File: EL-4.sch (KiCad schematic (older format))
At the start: 17 parts, among them J1 Conn_01x02, J2 Conn_01x03, Q1 BSS214NW, Q2 BSS214NW, U1 MIC4832

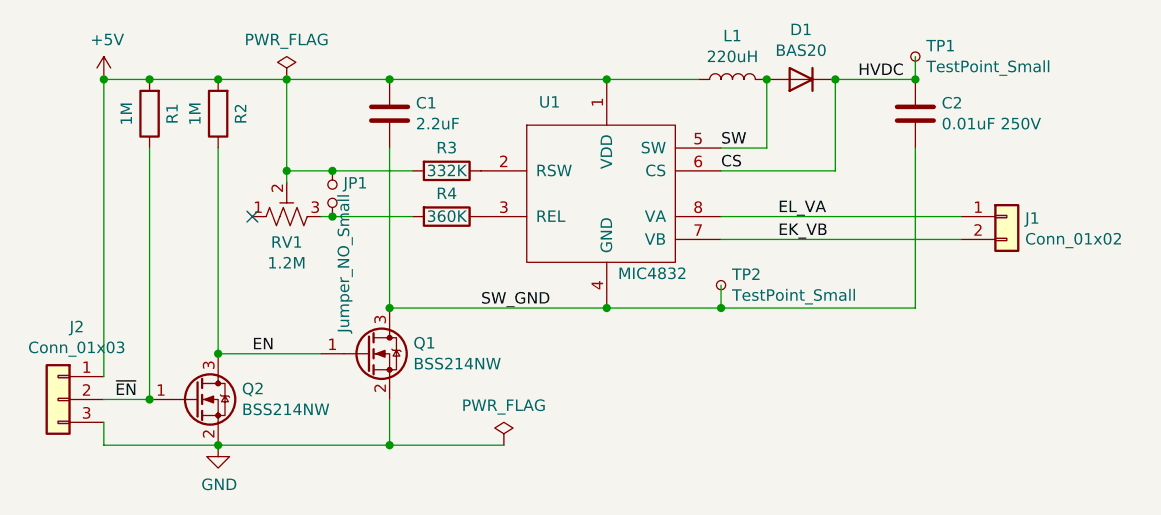
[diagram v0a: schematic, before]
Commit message: Version 1.0.
Changed enable method to pull RSW R3 to ground.
Changed R3, R4, R5 and C2 for 100Hz operation for 3 square inches.
Added input filter cap.

Also added BOM.

Signed-off-by: Aaron Williams <aaron.w2@gmail.com>
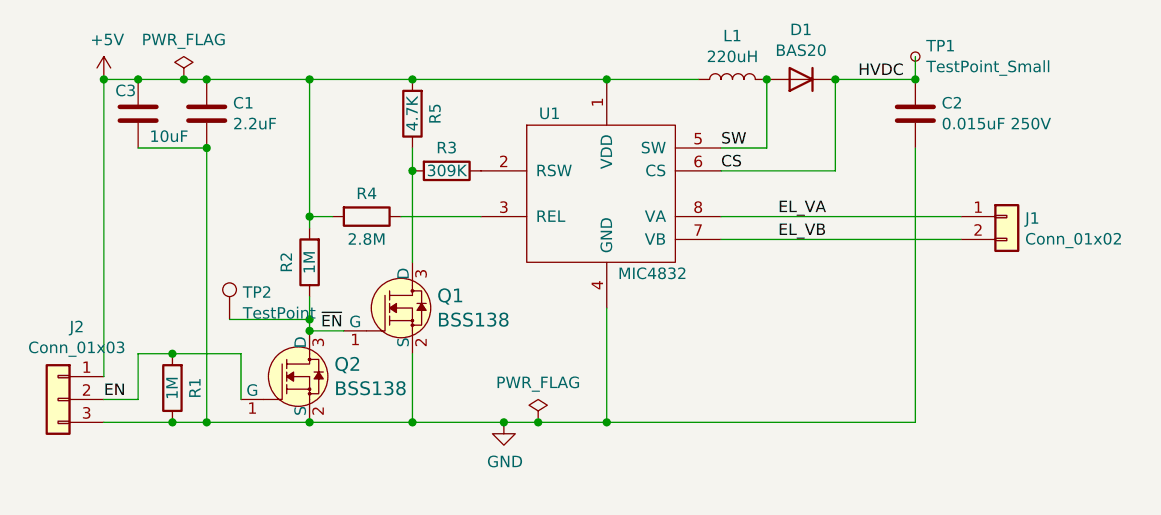
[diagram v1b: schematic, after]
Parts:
- removed JP1: Jumper_NO_Small, Jumper:SolderJumper-2_P1.3mm_Open_RoundedPad1.0x1.5mm, symbol Device:Jumper_NO_Small
- removed Q1, Q2: BSS214NW, Package_TO_SOT_SMD:SOT-323_SC-70, symbol Transistor_FET:BSS214NW
- removed RV1: 1.2M, Potentiometer_THT:Potentiometer_Bourns_3296W_Vertical, symbol Device:R_POT_TRIM_US
- removed TP2: TestPoint_Small, TestPoint:TestPoint_Pad_D1.0mm, symbol Connector:TestPoint_Small
- added C3: 10uF, Capacitor_SMD:C_0603_1608Metric, symbol Device:C
- added Q1, Q2: BSS138, Package_TO_SOT_SMD:SOT-23, symbol dk_Transistors-FETs-MOSFETs-Single:BSS138
- added R5: 4.7K, Resistor_SMD:R_0603_1608Metric, symbol Device:R
- added TP2: TestPoint, TestPoint:TestPoint_Pad_D1.0mm, symbol Connector:TestPoint
- C1: DESC (none) -> -; MFR (none) -> Yageo; MPN (none) -> CC0603MRY5V7BB225; SPN (none) -> 311-3415-1-ND; SPR (none) -> Digikey; SPURL (none) -> -
- C2: value 0.01uF 250V -> 0.015uF 250V; MPN C1206C103JAGACAUTO -> C1206C153KARECAUTO; SPN 80-C1206C103JAGAUTO -> 399-17899-1-ND; SPR Mouser -> Digikey; SPURL https://www.mouser.com/ProductDetail/KEMET/C1206C103JAGACAU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 -> https://www.digikey.com/en/products/detail/kemet/C1206C153K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
- D1: DESC (none) -> Diode Standard 200V 200mA Surface Mount SOT-23-3 (TO-236); MFR (none) -> ON Semiconductor; MPN (none) -> BAS20; SPN (none) -> BAS20FSCT-ND; SPR (none) -> Digikey; SPURL (none) -> https://www.digikey.com/en/products/detail/on-semiconductor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
- J1: DESC (none) -> Connector Header Through Hole 3 position 0.098; MFR (none) -> JST Sales America Inc.; MPN (none) -> B2B-XH-A-GU; SPN (none) -> 455-2946-ND; SPR (none) -> Digikey; SPURL (none) -> https://www.digikey.com/en/products/detail/jst-sales-americ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
- J2: DESC (none) -> Connector Header Through Hole 3 position 0.098; MFR (none) -> JST Sales America Inc.; MPN (none) -> B3B-XH-AM(LF)(SN); SPN (none) -> 455-2231-ND; SPR (none) -> Digikey; SPURL (none) -> https://www.digikey.com/en/products/detail/jst-sales-americ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
- L1: DESC (none) -> 220µH Semi-Shielded Wirewound Inductor 850mA 610mOhm Nonsta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; MFR (none) -> Bourns Inc.; MPN (none) -> SRN8040TA-221M; SPN (none) -> SRN8040TA-221MCT-ND; SPR (none) -> Digikey; SPURL (none) -> https://www.digikey.com/en/products/detail/bourns-inc/SRN80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
- R1, R2: DESC (none) -> 1 MOhms ±1% 0.1W, 1/10W Chip Resistor 0603 (1608 Metric) Au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; MFR (none) -> Stackpole Electronics Inc; MPN (none) -> RMCF0603FT1M00; SPN (none) -> RMCF0603FT1M00CT-ND; SPR (none) -> Digikey; SPURL (none) -> https://www.digikey.com/en/products/detail/stackpole-electr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
- R3: value 332K -> 309K; DESC (none) -> RES SMD 309K OHM 1% 1/10W 0603; MFR (none) -> Panasonic Electronic Components; MPN (none) -> ERJ-3EKF3093V; SPN (none) -> P309KHCT-ND; SPR (none) -> Digikey; SPURL (none) -> https://www.digikey.com/en/products/detail/panasonic-electr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
- R4: value 360K -> 2.8M; DESC (none) -> 2.8 MOhms ±1% 0.1W, 1/10W Chip Resistor 0603 (1608 Metric) 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; MFR Yageo -> Vishay Dale; MPN RC0603FR-07360KL -> CRCW06032M80FKEA; SPN (none) -> 541-2.80MHCT-ND; SPR (none) -> Digikey; SPURL (none) -> https://www.digikey.com/en/products/detail/CRCW06032M80FKEA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
- U1: DESC (none) -> EL Lamp Driver Controller 60Hz ~ 1kHz No 8-MSOP; MFR (none) -> Microchip Technology; SPR (none) -> Digikey; SPURL (none) -> https://www.digikey.com/en/products/detail/microchip-techno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
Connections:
- net SW_GND is gone; now on net GND: C1.2, C2.2, U1.4 (GND)
- net +5V: now also R4.2, C3.1, R5.2; no longer R1.2, R3.2
- net EN: now also J2.2 (Pin_2), R1.2, Q2.1 (G); no longer R2.1
- net GND: now also R1.1, C3.2, Q1.2 (S), Q2.2 (S)
- net ~EN: now also R2.1, Q1.1 (G), Q2.3 (D), TP2.1; no longer J2.2 (Pin_2), R1.1
- net EK_VB renamed EL_VB
- new net: Q1.3 (D), R3.2, R5.1
- no-connect marks 1 -> 0
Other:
- moved on the sheet: C1, R1, R4
